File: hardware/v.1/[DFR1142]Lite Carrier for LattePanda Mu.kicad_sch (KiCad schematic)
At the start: 6 parts

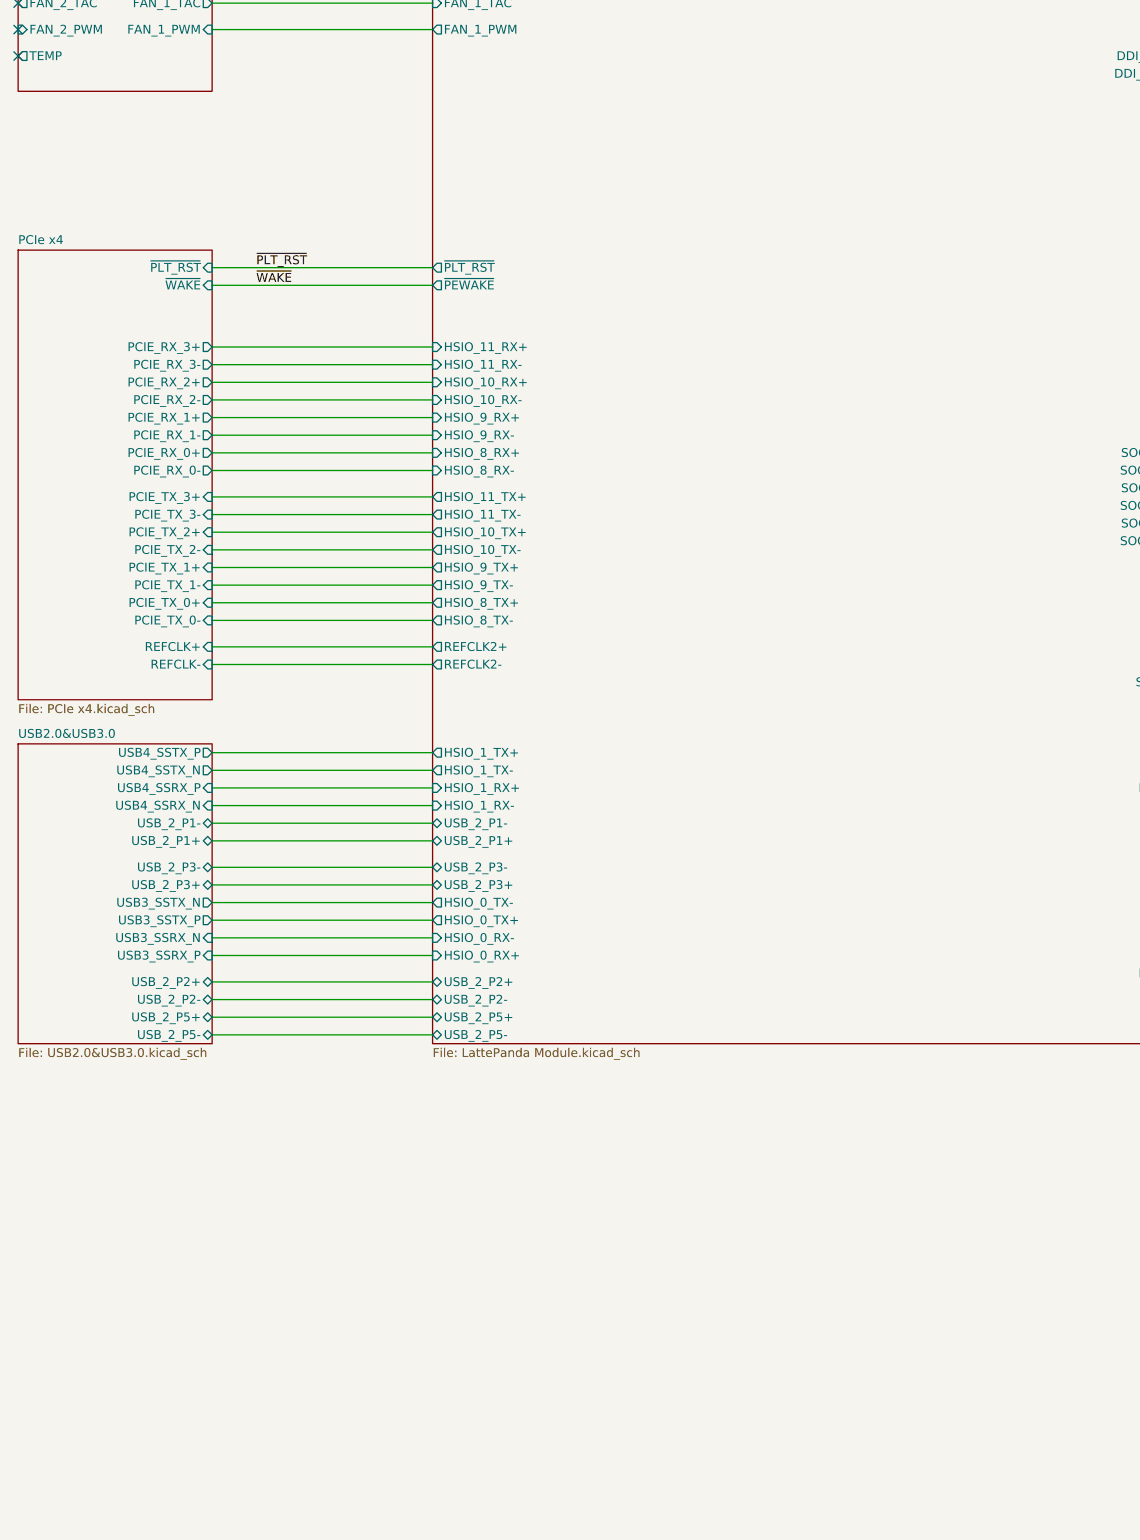
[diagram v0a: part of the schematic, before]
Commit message: pretty much finish the board, did bios chip, gpio, 4x sata
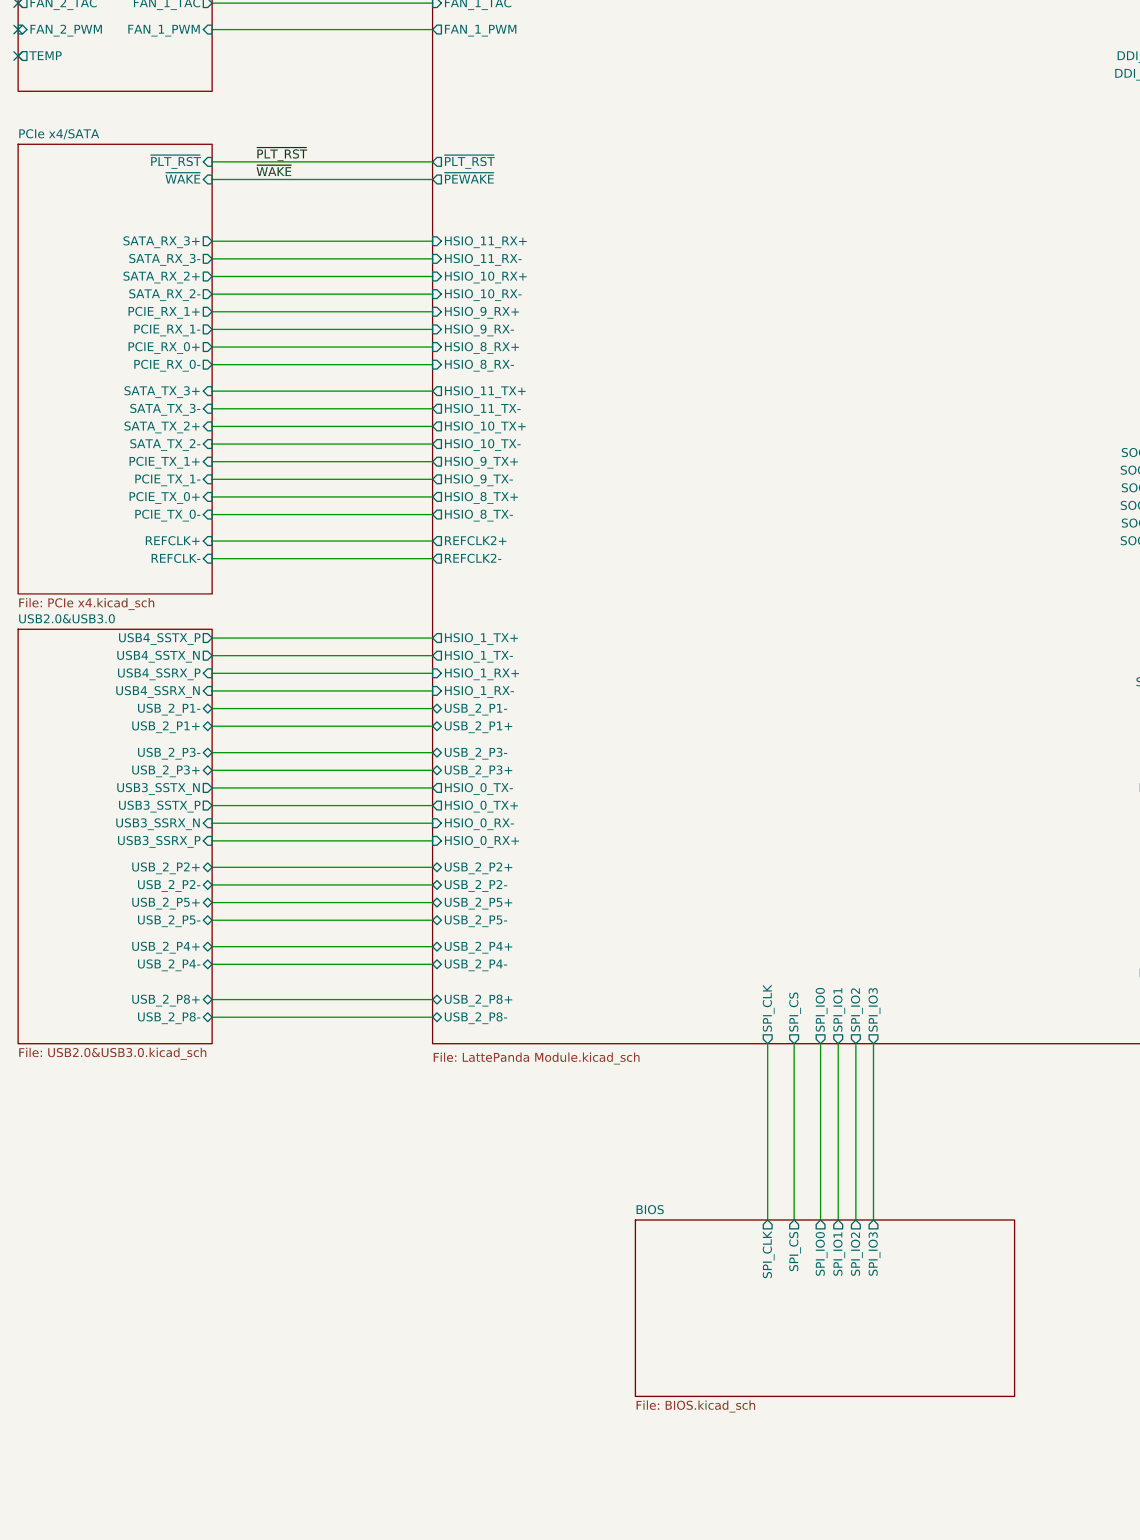
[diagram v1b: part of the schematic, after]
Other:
- sheet PCIe x4 renamed PCIe x4/SATA
- added sheet BIOS (BIOS.kicad_sch)
- sheet LattePanda Module ports: added SPI_CLK, SPI_CS, SPI_IO0, SPI_IO1, SPI_IO2, SPI_IO3, USB_2_P4+, USB_2_P4-, USB_2_P8+, USB_2_P8-; removed none
- sheet PCIe x4/SATA ports: added SATA_RX_2+, SATA_RX_2-, SATA_RX_3+, SATA_RX_3-, SATA_TX_2+, SATA_TX_2-, SATA_TX_3+, SATA_TX_3-; removed PCIE_RX_2+, PCIE_RX_2-, PCIE_RX_3+, PCIE_RX_3-, PCIE_TX_2+, PCIE_TX_2-, PCIE_TX_3+, PCIE_TX_3-
- sheet USB2.0&USB3.0 ports: added USB_2_P4+, USB_2_P4-, USB_2_P8+, USB_2_P8-; removed none

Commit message: add cad models for components, silkscreen labeling, fix asm1061 ground pour
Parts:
- H1, H2, H4: footprint A_HDJ_Library:MountingHole_3.2mm_M3_Pad_Via -> MountingHole_2.2mm_M2_DIN965_Pad
- H3: footprint A_HDJ_Library:MountingHole_3.2mm_M3_Pad_Via -> MountingHole:MountingHole_2.2mm_M2_DIN965_Pad
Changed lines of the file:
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@@
 			)
 		)
-		(property "Footprint" "A_HDJ_Library:MountingHole_3.2mm_M3_Pad_Via"
+		(property "Footprint" "MountingHole_2.2mm_M2_DIN965_Pad"
 			(at 473.71 336.55 0)
 			(effects
@@
 			)
 		)
-		(property "Footprint" "A_HDJ_Library:MountingHole_3.2mm_M3_Pad_Via"
+		(property "Footprint" "MountingHole_2.2mm_M2_DIN965_Pad"
 			(at 499.11 349.25 0)
 			(effects
@@
 			)
 		)
-		(property "Footprint" "A_HDJ_Library:MountingHole_3.2mm_M3_Pad_Via"
+		(property "Footprint" "MountingHole_2.2mm_M2_DIN965_Pad"
 			(at 473.71 349.25 0)
 			(effects
@@
 			)
 		)
-		(property "Footprint" "A_HDJ_Library:MountingHole_3.2mm_M3_Pad_Via"
+		(property "Footprint" "MountingHole:MountingHole_2.2mm_M2_DIN965_Pad"
 			(at 499.11 336.55 0)
 			(effects

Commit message: remove some footprints to use digikey ones
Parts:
- H1: footprint MountingHole_2.2mm_M2_DIN965_Pad -> MountingHole:MountingHole_3.2mm_M3_Pad_Via
- H2, H4: footprint MountingHole_2.2mm_M2_DIN965_Pad -> MountingHole:MountingHole_2.2mm_M2_DIN965_Pad
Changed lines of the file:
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@@
 			)
 		)
-		(property "Footprint" "MountingHole_2.2mm_M2_DIN965_Pad"
+		(property "Footprint" "MountingHole:MountingHole_3.2mm_M3_Pad_Via"
 			(at 473.71 336.55 0)
 			(effects
@@
 			)
 		)
-		(property "Footprint" "MountingHole_2.2mm_M2_DIN965_Pad"
+		(property "Footprint" "MountingHole:MountingHole_2.2mm_M2_DIN965_Pad"
 			(at 499.11 349.25 0)
 			(effects
@@
 			)
 		)
-		(property "Footprint" "MountingHole_2.2mm_M2_DIN965_Pad"
+		(property "Footprint" "MountingHole:MountingHole_2.2mm_M2_DIN965_Pad"
 			(at 473.71 349.25 0)
 			(effects
